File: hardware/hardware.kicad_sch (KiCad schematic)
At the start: 3 parts, among them J2 USB_C_Receptacle

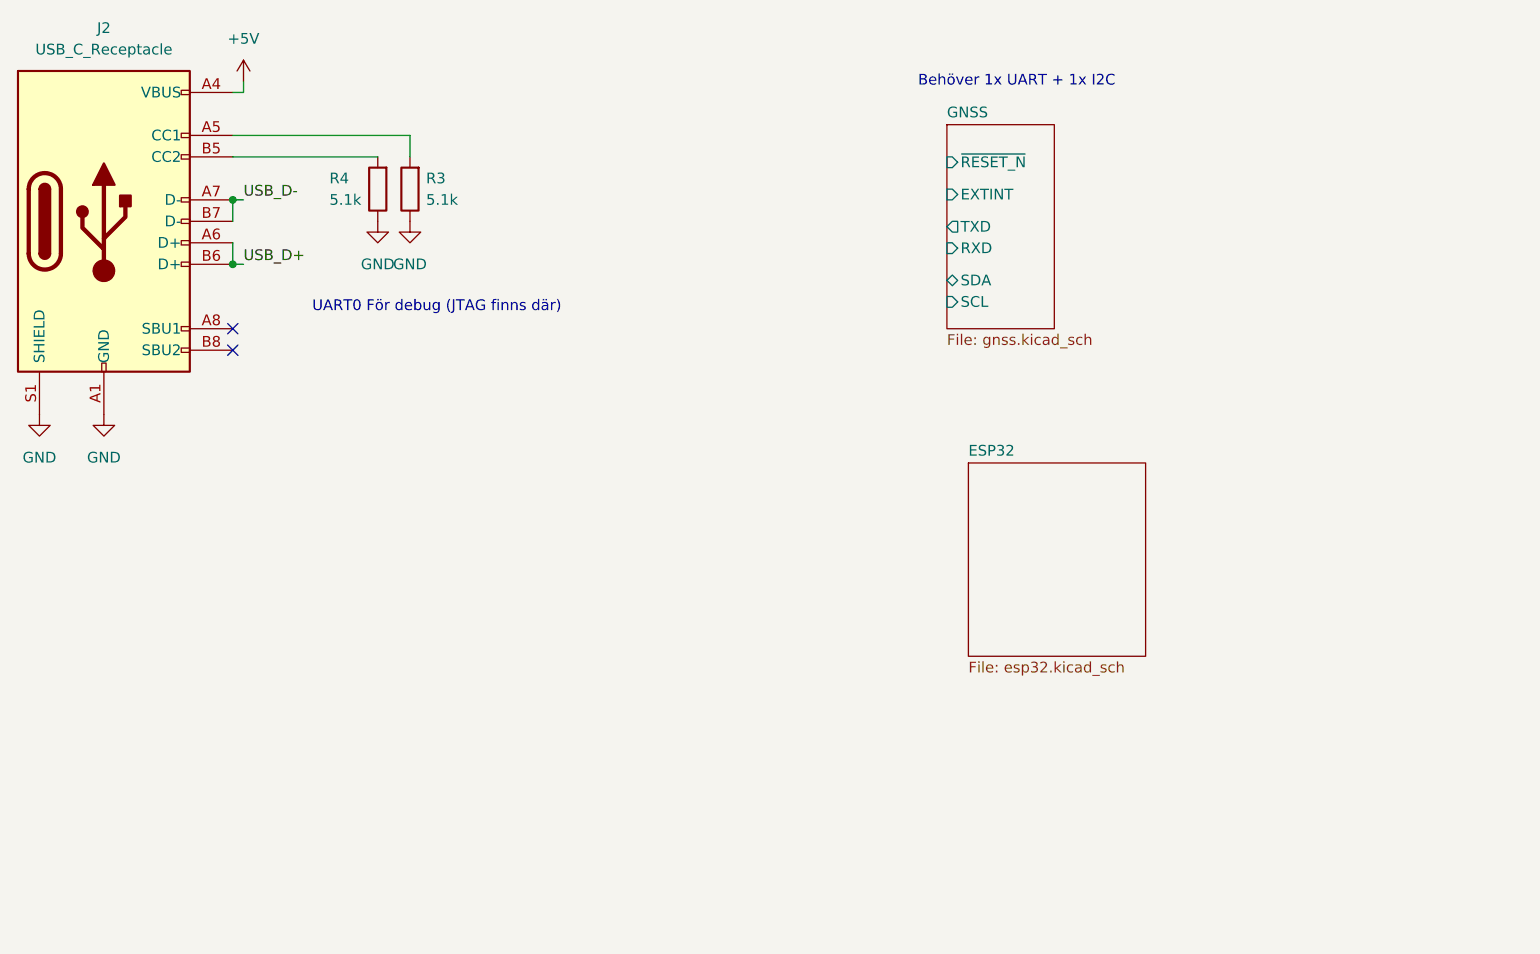
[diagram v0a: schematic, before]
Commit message: new symbol + some buses
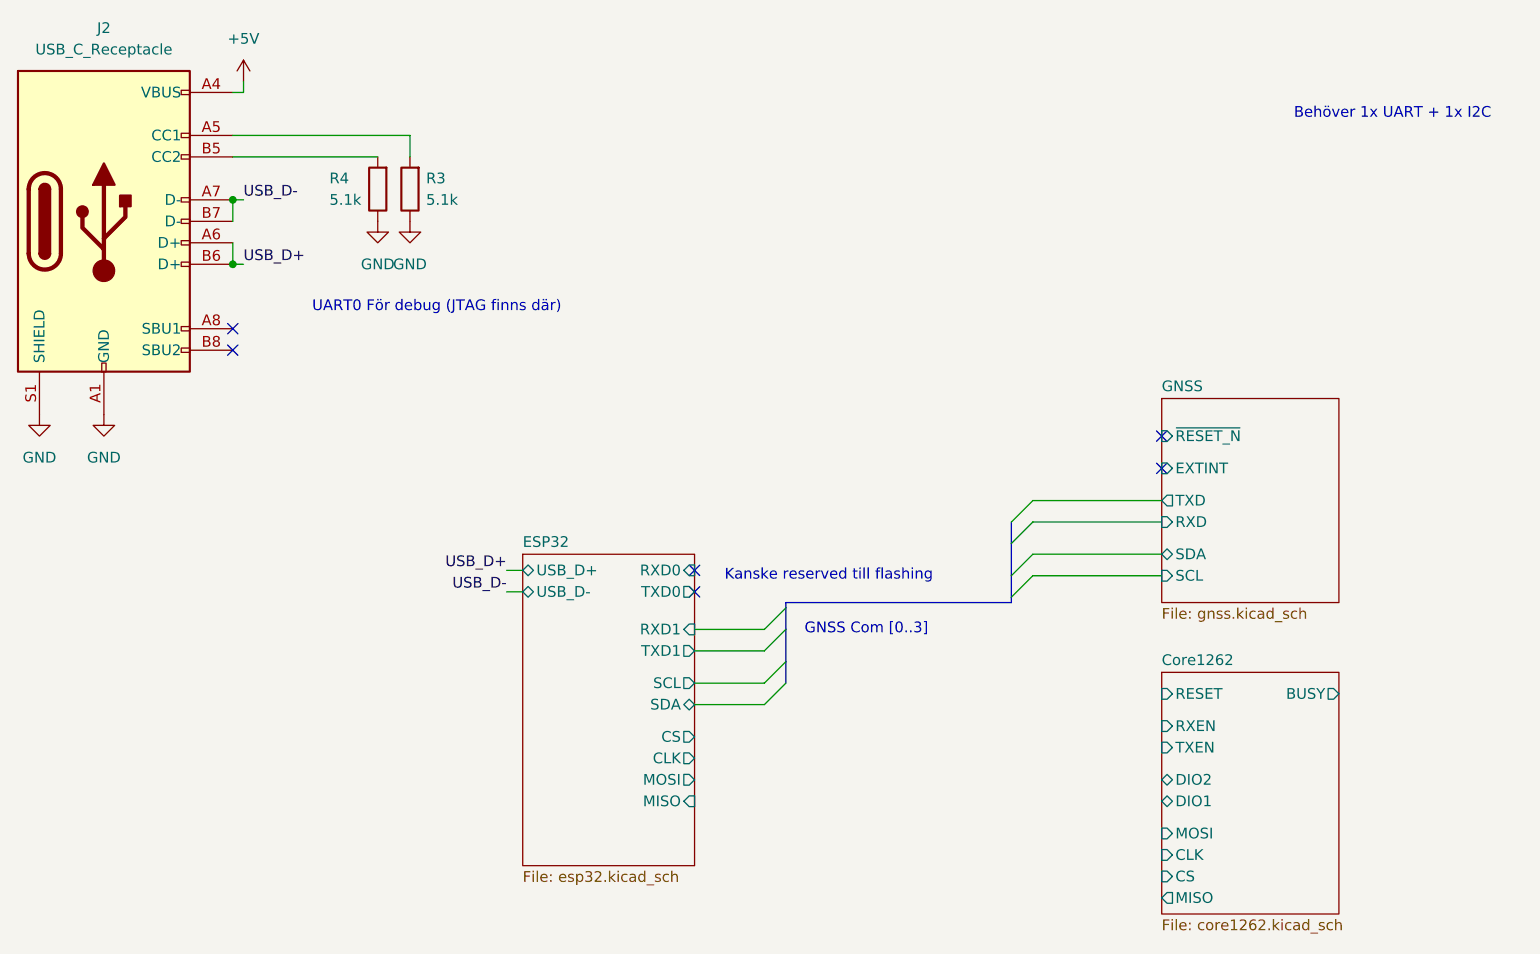
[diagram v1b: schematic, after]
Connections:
- no-connect marks 2 -> 6
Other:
- added sheet Core1262 (core1262.kicad_sch)
- sheet ESP32 ports: added CLK, CS, MISO, MOSI, RXD0, RXD1, SCL, SDA, TXD0, TXD1, USB_D+, USB_D-; removed none
- note added: "GNSS Com [0..3]"
- note added: "Kanske reserved till flashing"
